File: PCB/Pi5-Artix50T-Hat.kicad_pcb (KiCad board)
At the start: 4 copper layers, 85 x 56 mm, 162 parts, among them J1 GPIO, J2 Molex 0878321420, J3 68711614522, J5 MIPI0, J6 MIPI1, U1 BL24C256A, U10 AP62200TWU-7, U11 AP62200TWU-7, U12 AP62200TWU-7, U2 XC7A50T-FGG484, U9 AP62200TWU-7, X1 50MHz

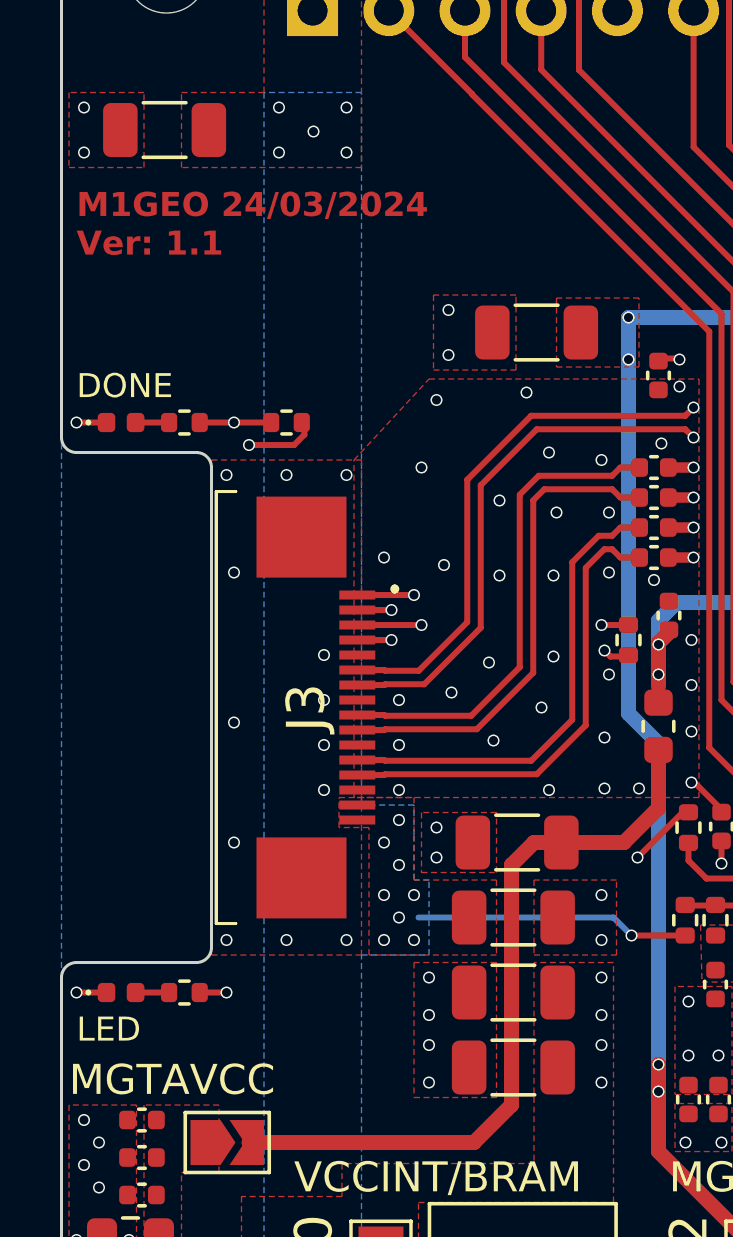
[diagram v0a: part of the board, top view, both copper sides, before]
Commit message: Updating LEDs footprint and Resistors value
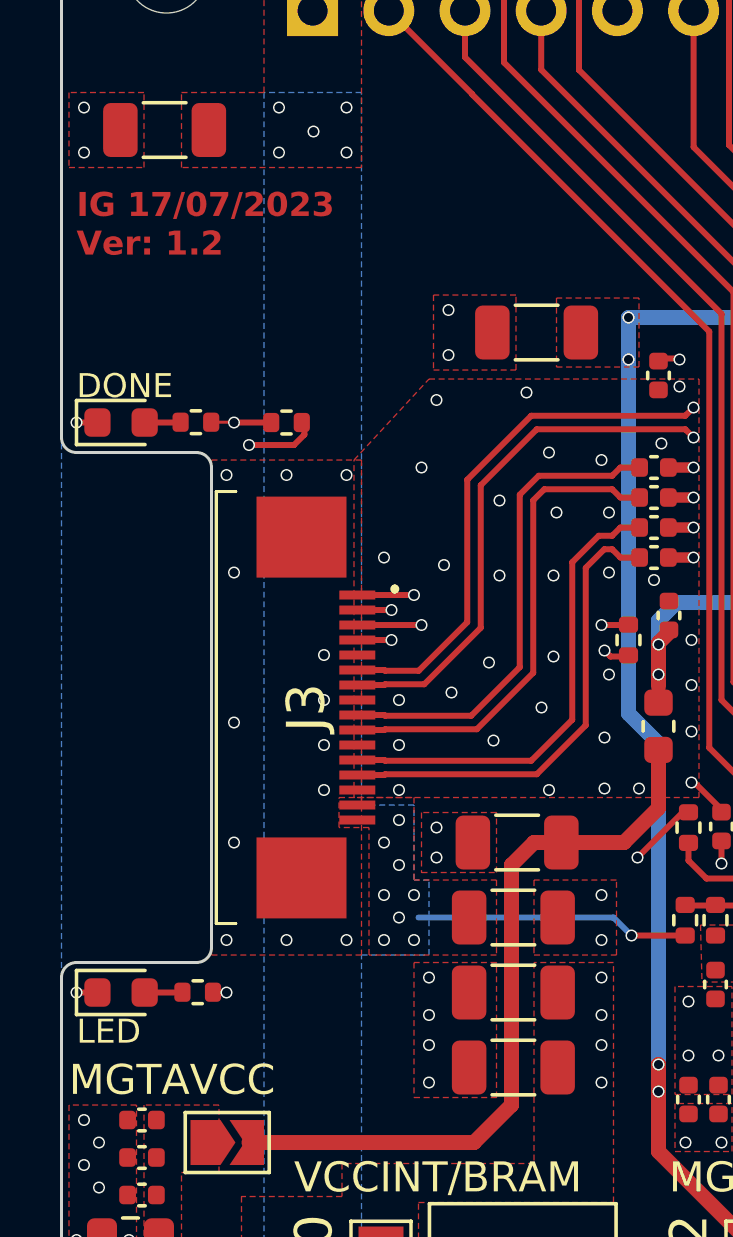
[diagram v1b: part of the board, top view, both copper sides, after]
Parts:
- D1, D2: footprint LED_SMD:LED_0402_1005Metric -> LED_SMD:LED_0603_1608Metric
- J5: value MIPI0 -> C597981
- J6: value MIPI1 -> C597981
- R1, R17, R19, R2, R3, R5, R6, R7, R8, R9: value 3.2k -> 4k7
- moved R18 0.44 mm to (104.5, 81.5)
- moved R11 0.38 mm to (104.5, 62.5)
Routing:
- net /FPGA Top/FPGA_LED: track 24.3 -> 23.5 mm
- net Net-(D2-A): track 1.03 -> 1.56 mm
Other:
- board text added: "IG 17/07/2023 Ver: 1.2"
- board text removed: "M1GEO 24/03/2024 Ver: 1.1"

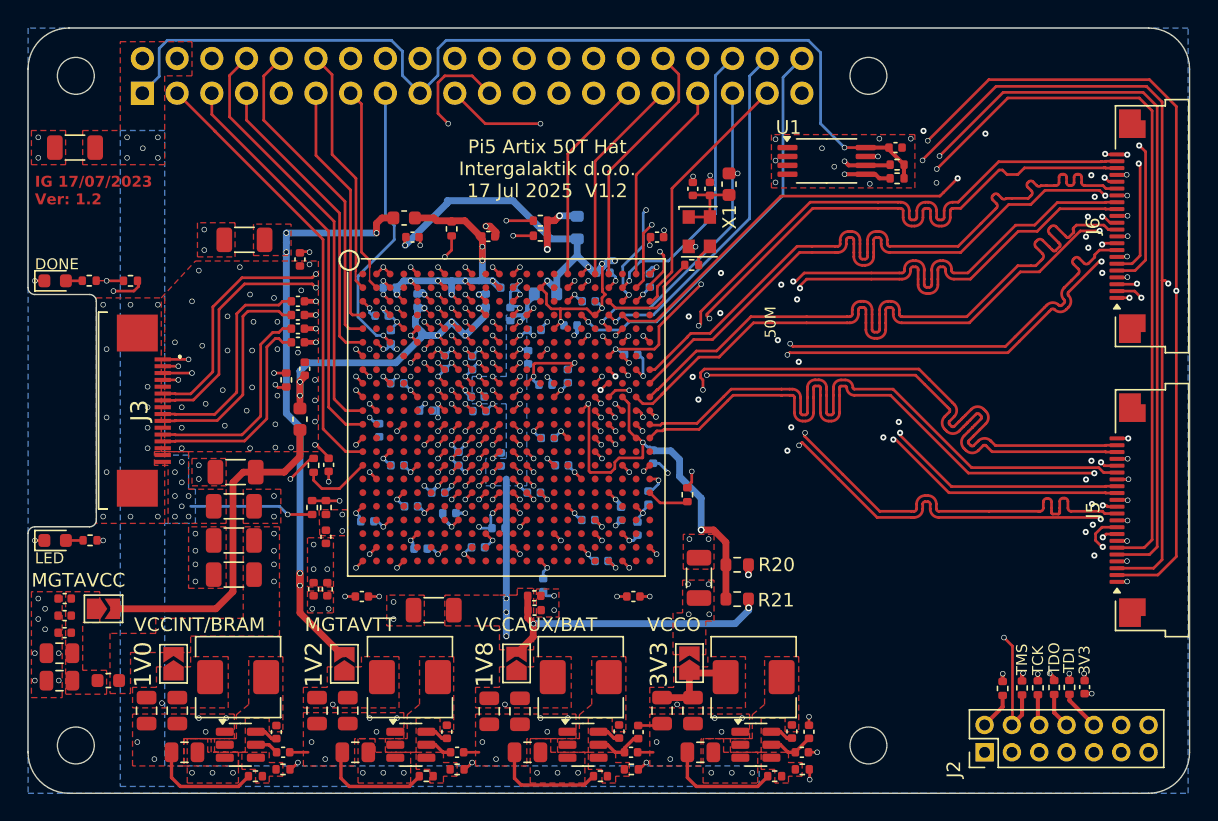
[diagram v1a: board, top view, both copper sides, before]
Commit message: updating connector
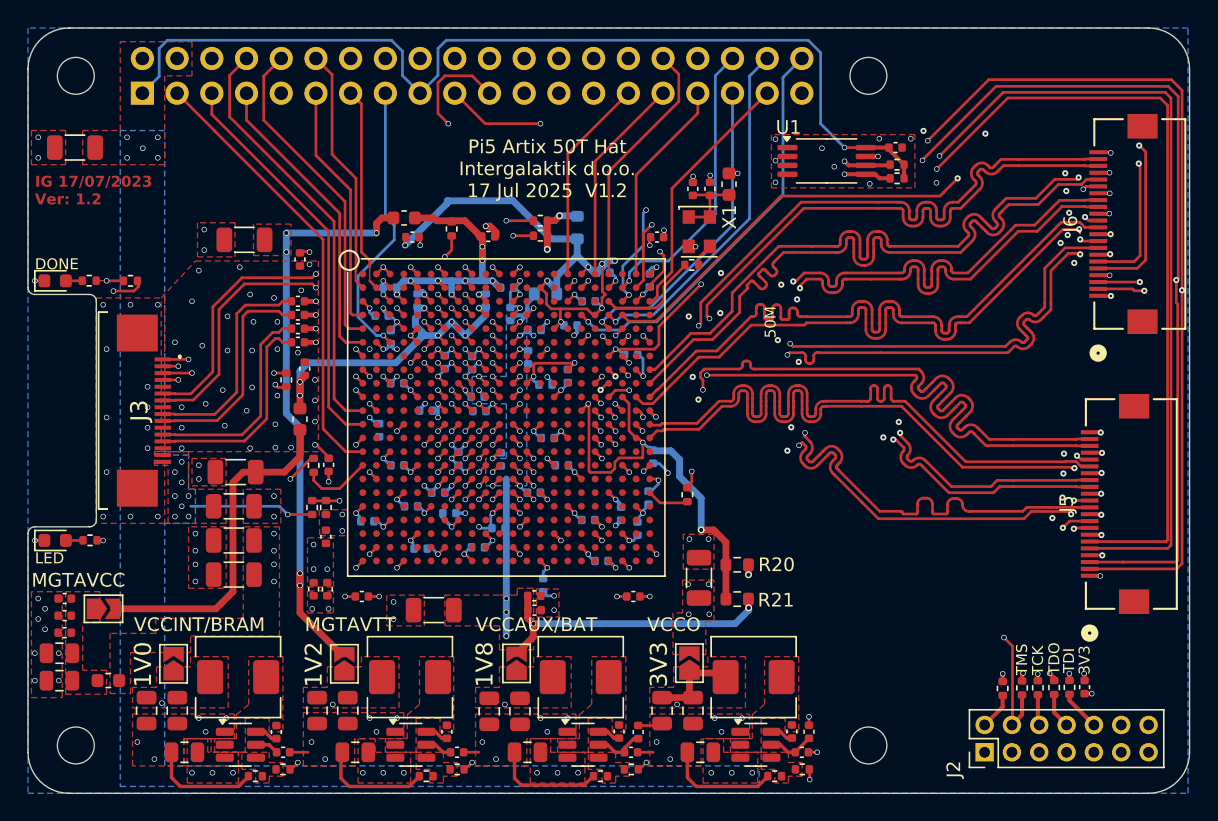
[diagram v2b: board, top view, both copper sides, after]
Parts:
- J5, J6: footprint Connector_FFC-FPC:Amphenol_F32Q-1A7x1-11022_1x22-1MP_P0.5mm_Horizontal -> FHT12:CONN_FH12-22S-0.5SH55_HIR
- moved J5 1.90 mm to (180.7, 78.8)
- moved J6 1.24 mm to (181.4, 58.3)
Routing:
- net /FPGA Top/FPGA Bank 15 & 16/MIPI0_D1-: track 47.0 -> 39.3 mm
- net /FPGA Top/FPGA Bank 15 & 16/MIPI0_D1+: track 47.1 -> 40.2 mm
- net /FPGA Top/FPGA Bank 15 & 16/SCL0: track 95.6 -> 101.6 mm
- net /FPGA Top/FPGA Bank 15 & 16/SDA0: track 99.2 -> 104.3 mm
- net /FPGA Top/FPGA Bank 15 & 16/MIPI0_CAM_GPIO0: track 80.1 -> 84.4 mm
- net /FPGA Top/FPGA Bank 15 & 16/MIPI0_CAM_GPIO1: track 84.6 -> 88.7 mm
- net /FPGA Top/FPGA Bank 15 & 16/MIPI1_D3+: track 46.9 -> 50.4 mm, vias 2 -> 0
- net /FPGA Top/FPGA Bank 15 & 16/MIPI0_D3-: track 46.4 -> 49.7 mm
- net /FPGA Top/FPGA Bank 15 & 16/MIPI1_D1+: track 44.3 -> 47.0 mm
- net /FPGA Top/FPGA Bank 15 & 16/MIPI1_CK-: track 47.3 -> 49.1 mm
- net /FPGA Top/FPGA Bank 15 & 16/MIPI1_D3-: track 49.6 -> 47.7 mm, vias 0 -> 2
- net BANK_15_VCC: track 120.0 -> 121.4 mm
- net /FPGA Top/FPGA Bank 15 & 16/MIPI1_CAM_GPIO1: track 52.5 -> 53.8 mm
- net /FPGA Top/FPGA Bank 15 & 16/MIPI1_CAM_GPIO0: track 51.5 -> 52.8 mm
- net GND: track 165.7 -> 166.9 mm, vias 259 -> 256
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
